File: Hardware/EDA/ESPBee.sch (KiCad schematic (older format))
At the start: 8 parts, among them P1 HEADER_M_XBEE_P1-P10_PTH_DTE, P2 HEADER_M_XBEE_P11-P20_PTH_DTE, U1 ESP-12E

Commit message: Fixed connections and added pull-up/down resistors for configuration pins.
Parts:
- removed U1: ESP-12E, RF_Modules:ESP-12E, symbol ESP-12E-RESCUE-ESPBee
- added R1, R2, R3, R4: 10K, Passive:R0603, symbol RES_Small
- added U1: ESP-12E, RF_Modules:ESP-12E, symbol ESP-12E
- P1: value HEADER_M_XBEE_P1-P10_PTH_DTE -> XBEE HEADER
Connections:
- net labels added: UPLOAD
- wire segments 24 -> 41
- no-connect marks 30 -> 25
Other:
- note added: "GPIO0 Low = Bootloader\nGPIO0 High = Boot from flash"
- note added: "GPIO15 needs to be pulled low for ESP to respond to UART commands"
- note added: "GPIO2 = Recovery mode when pulled low 2s after boot"
- moved on the sheet: C1, C2, C3, C4

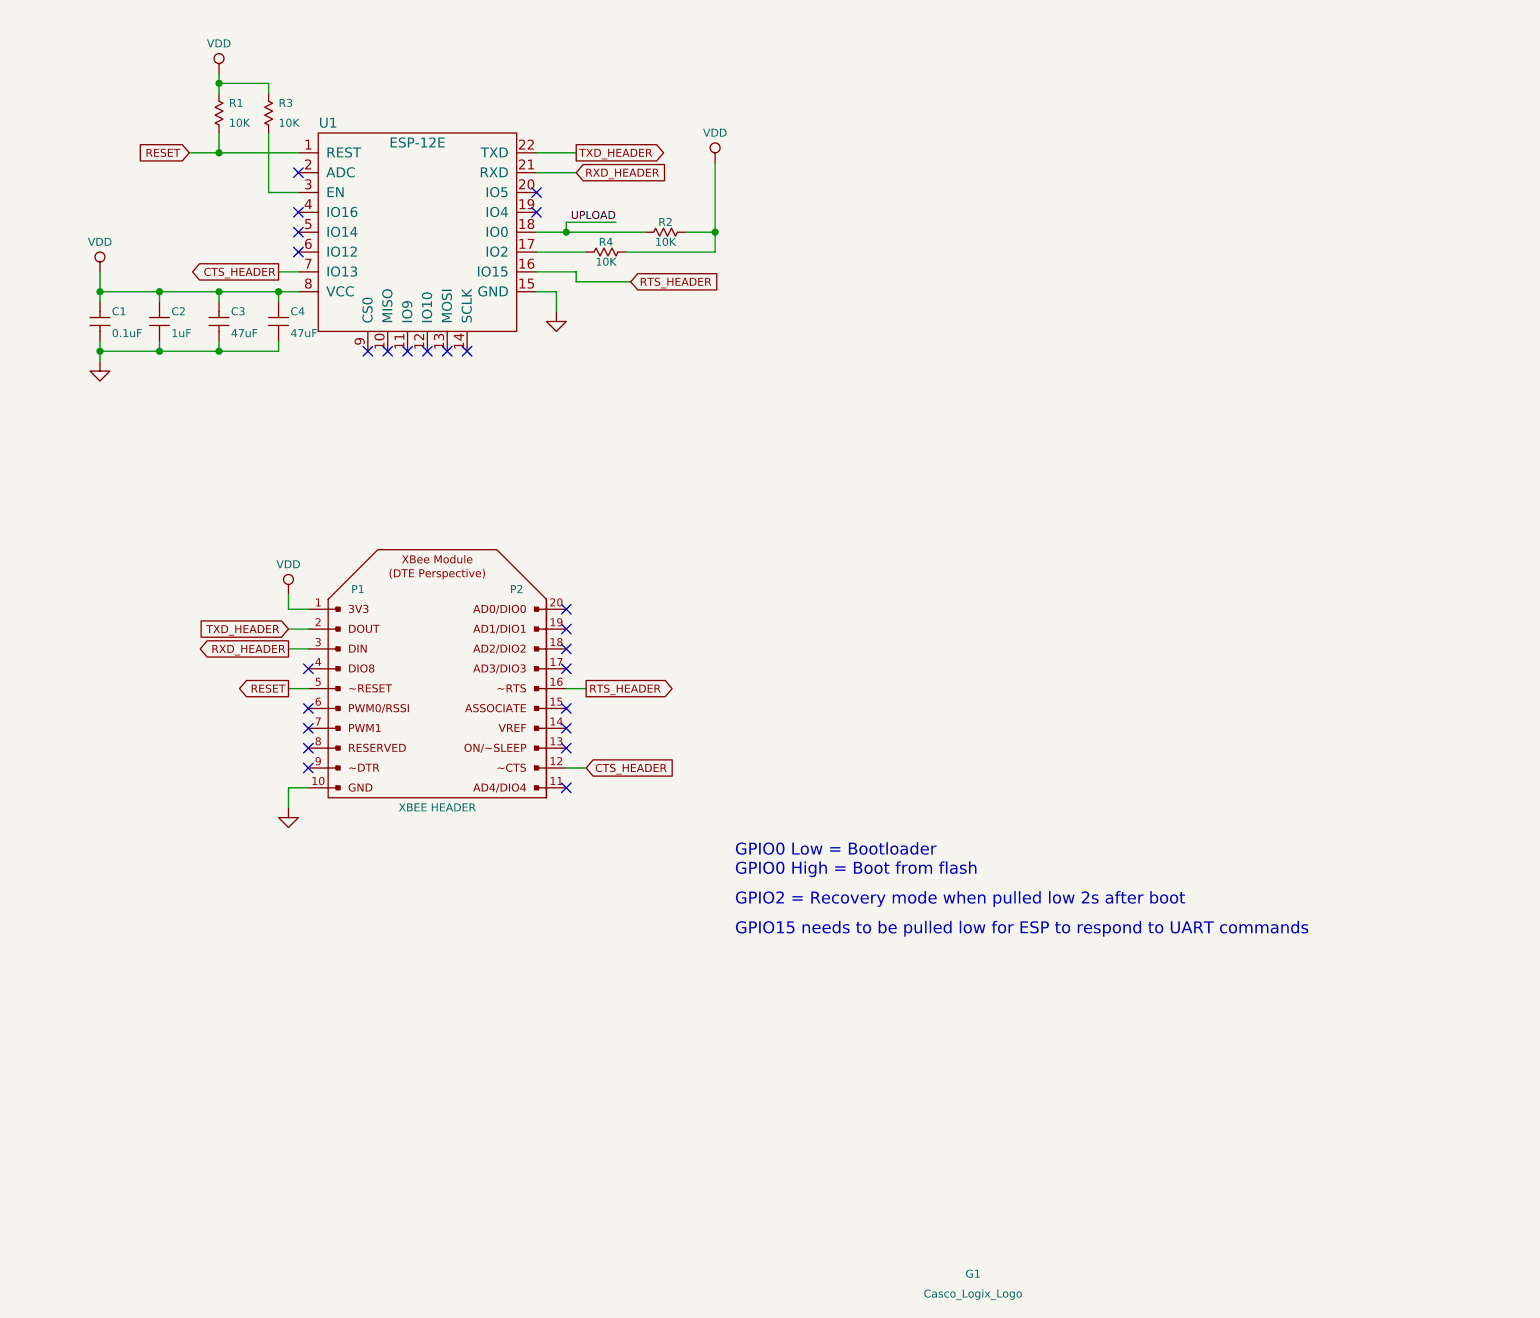
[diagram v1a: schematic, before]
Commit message: Updated schematic and board layout to include ON/SLEEP signal. Generated new gerber files.
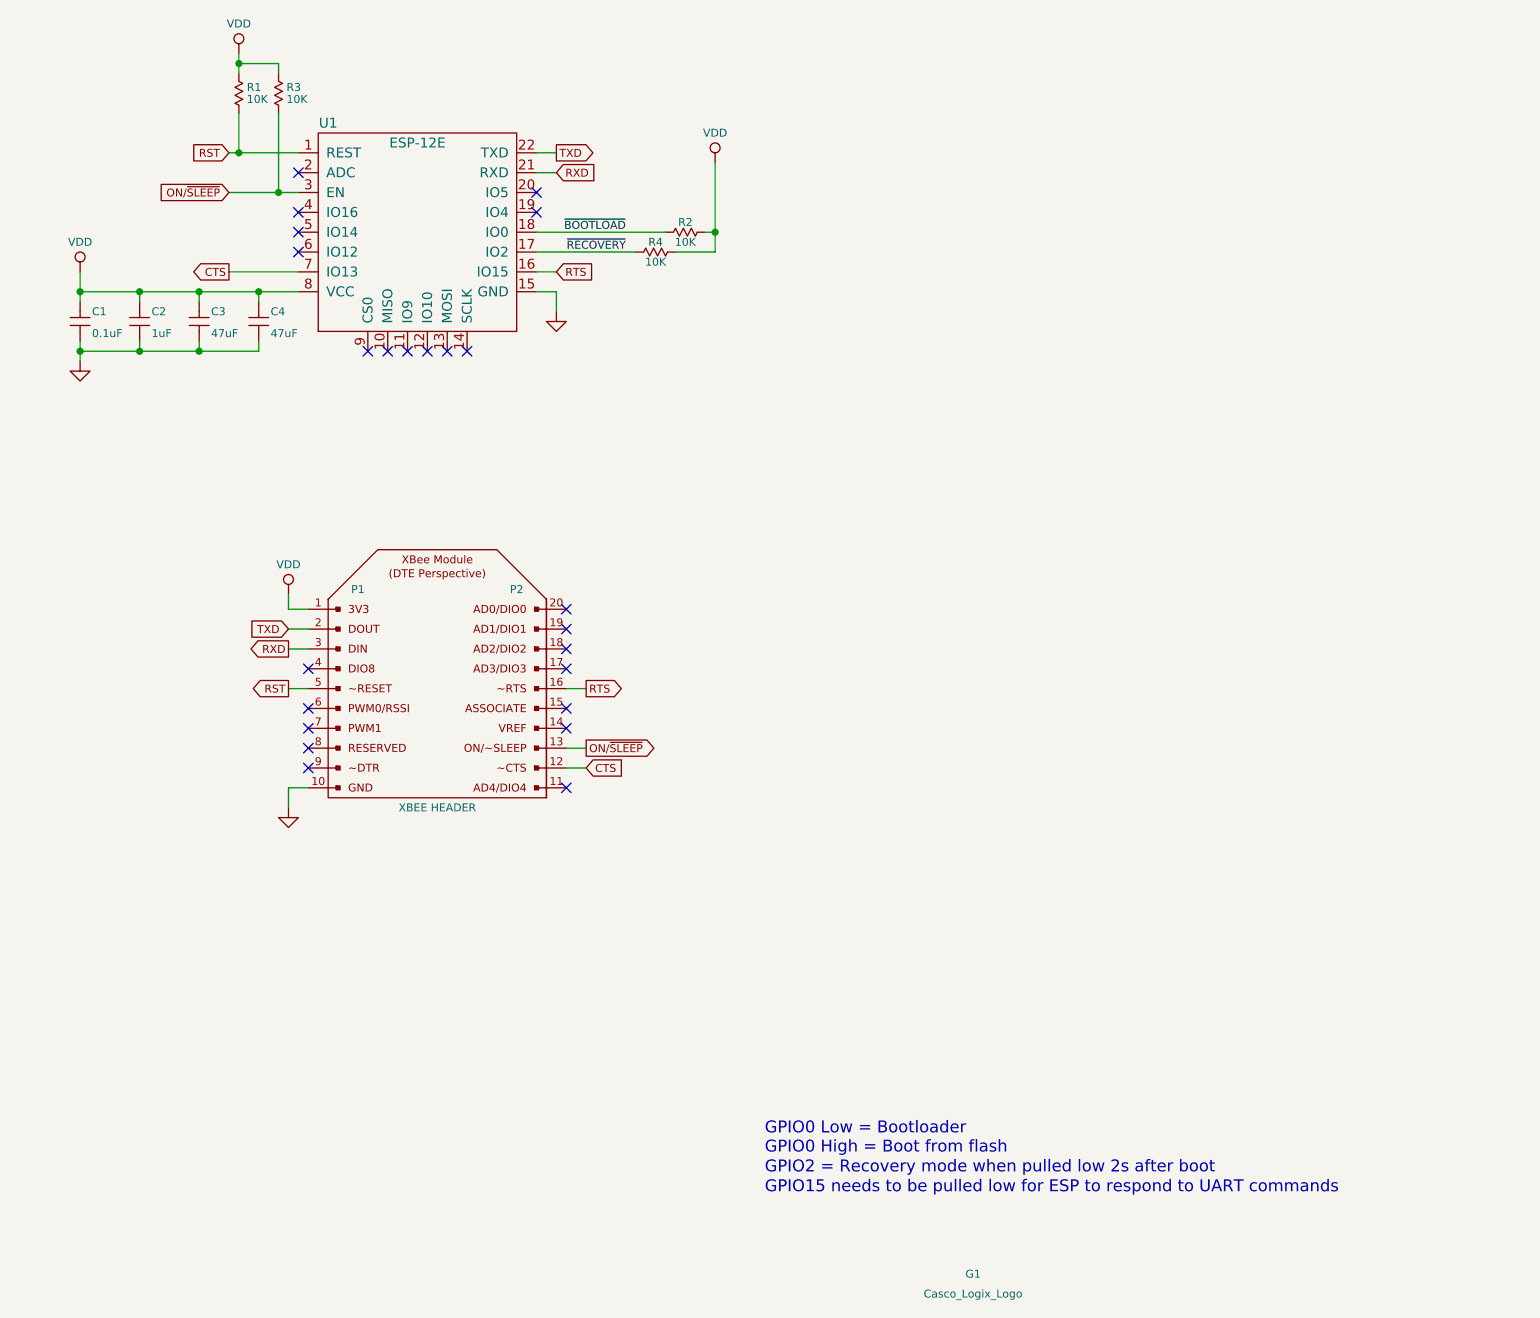
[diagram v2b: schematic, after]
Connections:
- net ON/~SLEEP: now reaches P2.13 (GPIO2)
- net ON/~SLEEP: now also R3.2, U1.3 (EN)
- net ~RECOVERY: now reaches R4.2, U1.17 (IO2)
- net CTS_HEADER renamed CTS
- net RESET renamed RST
- net RTS_HEADER renamed RTS
- net RXD_HEADER renamed RXD
- net TXD_HEADER renamed TXD
- net UPLOAD renamed ~BOOTLOAD
- no-connect marks 25 -> 24
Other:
- moved on the sheet: C1, C2, C3, C4, R1, R2, R3, R4
